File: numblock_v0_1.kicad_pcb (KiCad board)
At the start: 2 copper layers, 100 x 100 mm, 66 parts, among them J1 Conn_01x14_Female, J2 Conn_01x14_Female, J3 Conn_01x05_Female, J4 Conn_02x03_Odd_Even, J5 Conn_01x03_Female, SW1 SW_PUSH-MX_W_LED, SW10 SW_PUSH-MX_W_LED, SW11 SW_PUSH-MX_W_LED, SW12 SW_PUSH-MX_W_LED, SW13 SW_PUSH-MX_W_LED, SW14 SW_PUSH-MX_W_LED, SW15 SW_PUSH-MX_W_LED, SW16 SW_PUSH-MX_W_LED, SW17 SW_PUSH-MX_W_LED, SW18 SW_PUSH-MX_W_LED, SW19 SW_PUSH-MX_W_LED, SW2 SW_PUSH-MX_W_LED, SW20 SW_PUSH-MX_W_LED, SW21 Rotary_Encoder_Switch, SW3 SW_PUSH-MX_W_LED, SW4 SW_PUSH-MX_W_LED, SW5 SW_PUSH-MX_W_LED, SW6 SW_PUSH-MX_W_LED, SW7 SW_PUSH-MX_W_LED, SW8 SW_PUSH-MX_W_LED, SW9 SW_PUSH-MX_W_LED

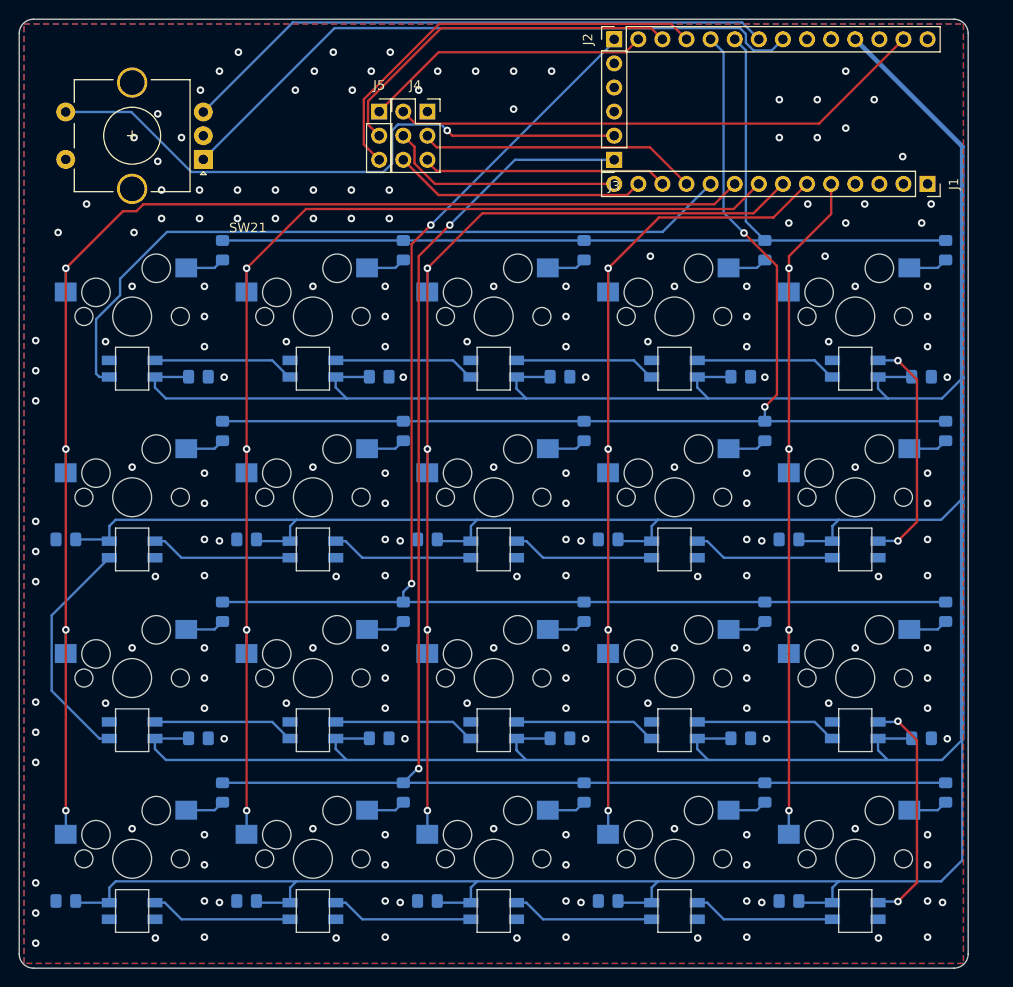
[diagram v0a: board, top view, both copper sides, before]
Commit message: Fixed missing gnd connections
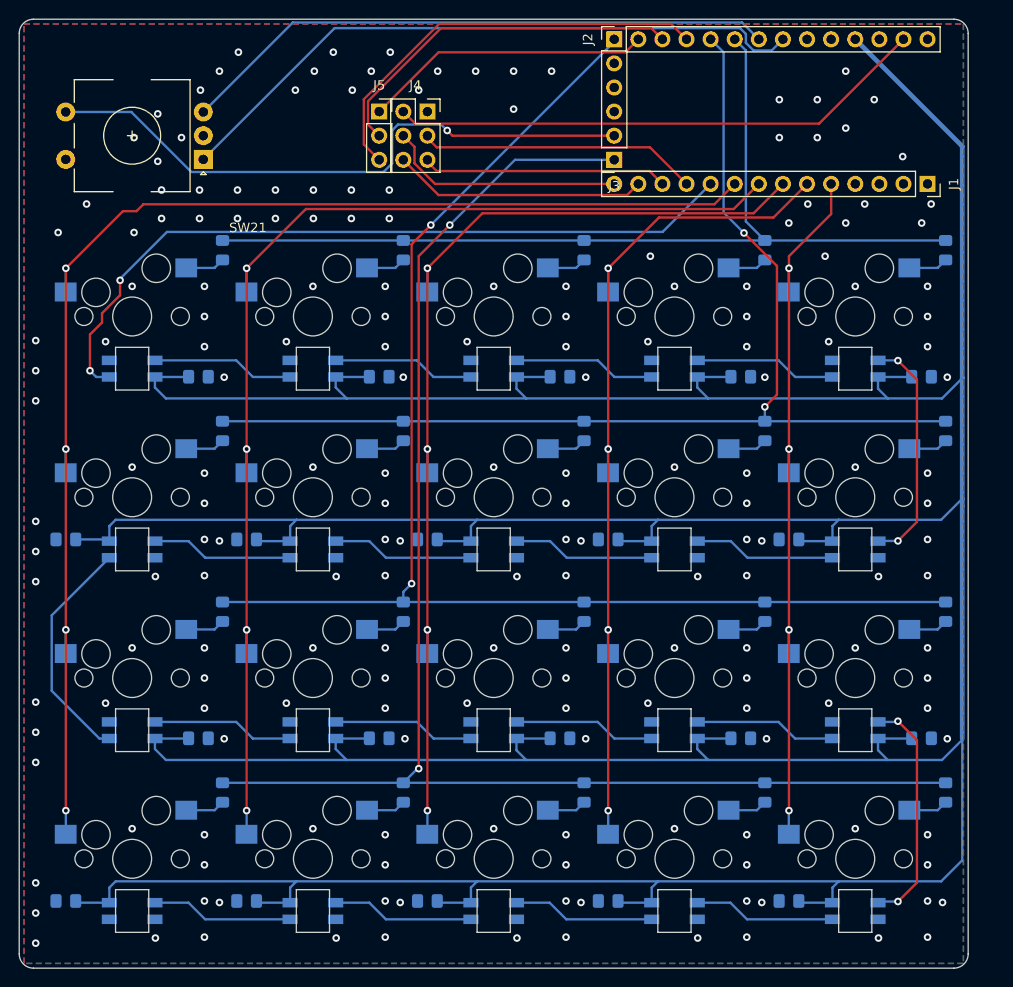
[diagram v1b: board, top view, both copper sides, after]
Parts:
- SW21: footprint Rotary_Encoder:RotaryEncoder_Alps_EC11E-Switch_Vertical_H20mm_CircularMountingHoles -> sofle RGB:RotaryEncoder_Alps_EC11E-Switch_Vertical_H20mm_NoMountingHoles
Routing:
- net /LED: track 79.0 -> 79.5 mm, vias 0 -> 2
- net GND: vias 162 -> 163
- net /R2: vias 3 -> 2

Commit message: kinda done, about to add jumpers for rot. enc.
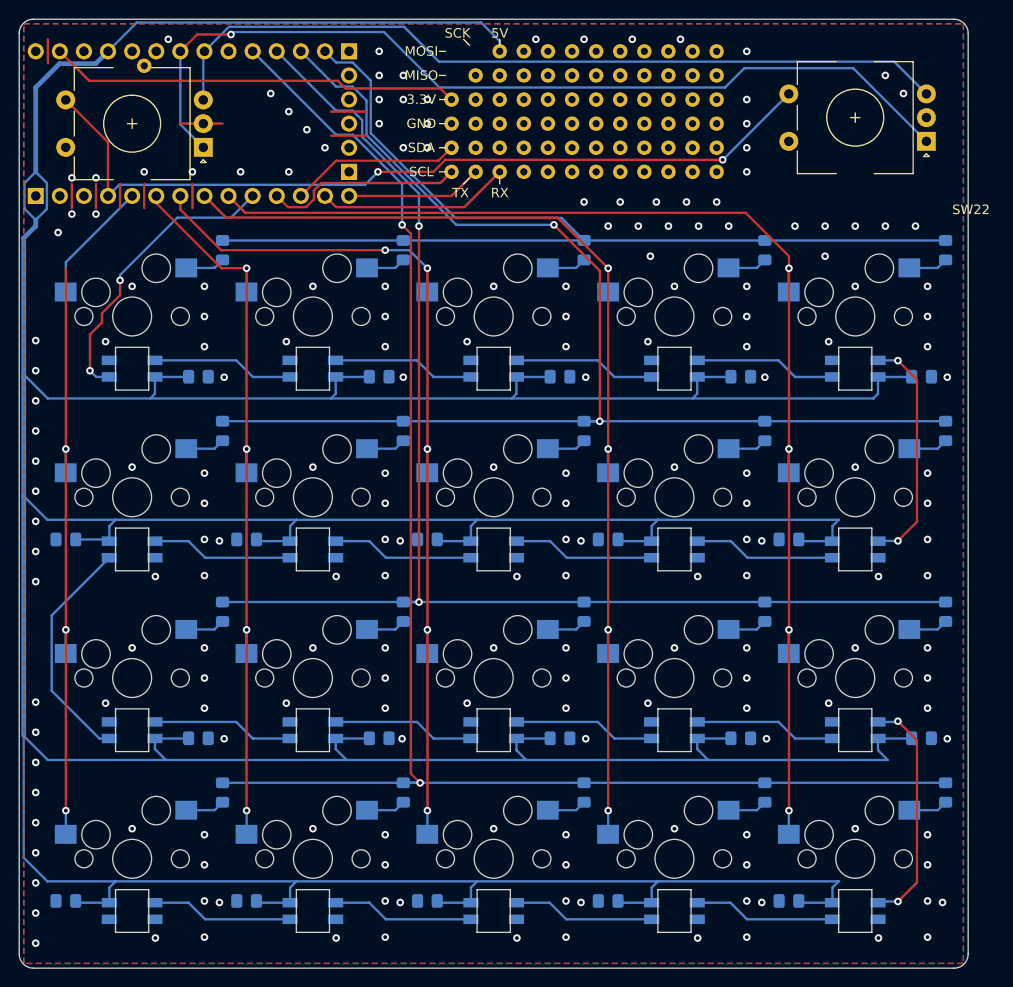
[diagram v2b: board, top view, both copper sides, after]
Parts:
- removed the C1 at (31.1, 118.7)
- removed the C10 at (121.3, 101.6)
- removed the C2 at (50.2, 118.7)
- removed the C3 at (69.2, 118.7)
- removed the C4 at (88.3, 118.7)
- removed the C5 at (107.3, 118.7)
- removed the C6 at (45.1, 101.6)
- removed the C7 at (64.1, 101.6)
- removed the C8 at (83.2, 101.6)
- removed the C9 at (102.2, 101.6)
- removed J4: Conn_02x03_Odd_Even, Connector_PinSocket_2.54mm:PinSocket_2x03_P2.54mm_Vertical
- removed J5: Conn_01x03_Female, Connector_PinSocket_2.54mm:PinSocket_1x03_P2.54mm_Vertical
- added C11: C, Capacitor_SMD:C_0805_2012Metric_Pad1.18x1.45mm_HandSolder, B.Cu at (45.1, 101.6)
- added C12: C, Capacitor_SMD:C_0805_2012Metric_Pad1.18x1.45mm_HandSolder, B.Cu at (64.1, 101.6)
- added C13: C, Capacitor_SMD:C_0805_2012Metric_Pad1.18x1.45mm_HandSolder, B.Cu at (102.2, 101.6)
- added C14: C, Capacitor_SMD:C_0805_2012Metric_Pad1.18x1.45mm_HandSolder, B.Cu at (83.2, 101.6)
- added C15: C, Capacitor_SMD:C_0805_2012Metric_Pad1.18x1.45mm_HandSolder, B.Cu at (121.3, 101.6)
- added C16: C, Capacitor_SMD:C_0805_2012Metric_Pad1.18x1.45mm_HandSolder, B.Cu at (31.1, 118.7)
- added C17: C, Capacitor_SMD:C_0805_2012Metric_Pad1.18x1.45mm_HandSolder, B.Cu at (50.2, 118.7)
- added C18: C, Capacitor_SMD:C_0805_2012Metric_Pad1.18x1.45mm_HandSolder, B.Cu at (69.2, 118.7)
- added C19: C, Capacitor_SMD:C_0805_2012Metric_Pad1.18x1.45mm_HandSolder, B.Cu at (88.3, 118.7)
- added C20: C, Capacitor_SMD:C_0805_2012Metric_Pad1.18x1.45mm_HandSolder, B.Cu at (107.3, 118.7)
- added H1: MountingHole_Pad, sofle RGB:hole_30mil, F.Cu at (71.8, 36.8)
- added H2: MountingHole_Pad, sofle RGB:hole_30mil, F.Cu at (71.8, 34.3)
- added H3: MountingHole_Pad, sofle RGB:hole_30mil, F.Cu at (71.8, 39.4)
- added H4: MountingHole_Pad, sofle RGB:hole_30mil, F.Cu at (71.8, 41.9)
- added H5: MountingHole_Pad, sofle RGB:hole_30mil, F.Cu at (74.3, 41.9)
- added H6: MountingHole_Pad, sofle RGB:hole_30mil, F.Cu at (76.8, 41.9)
- added REF**: hole_30mil, sofle RGB:hole_30mil, F.Cu at (39.4, 30.7)
- added REF**: hole_30mil, sofle RGB:hole_30mil, F.Cu at (87.0, 41.9)
- added REF**: hole_30mil, sofle RGB:hole_30mil, F.Cu at (84.5, 41.9)
- added REF**: hole_30mil, sofle RGB:hole_30mil, F.Cu at (81.9, 41.9)
- added REF**: hole_30mil, sofle RGB:hole_30mil, F.Cu at (79.4, 41.9)
- added REF**: hole_30mil, sofle RGB:hole_30mil, F.Cu at (74.3, 39.4)
- added REF**: hole_30mil, sofle RGB:hole_30mil, F.Cu at (99.7, 39.4)
- added REF**: hole_30mil, sofle RGB:hole_30mil, F.Cu at (97.2, 39.4)
- added REF**: hole_30mil, sofle RGB:hole_30mil, F.Cu at (94.6, 39.4)
- added REF**: hole_30mil, sofle RGB:hole_30mil, F.Cu at (92.1, 39.4)
- added REF**: hole_30mil, sofle RGB:hole_30mil, F.Cu at (89.5, 39.4)
- added REF**: hole_30mil, sofle RGB:hole_30mil, F.Cu at (74.3, 34.3)
- added REF**: hole_30mil, sofle RGB:hole_30mil, F.Cu at (87.0, 39.4)
- added REF**: hole_30mil, sofle RGB:hole_30mil, F.Cu at (84.5, 39.4)
- added REF**: hole_30mil, sofle RGB:hole_30mil, F.Cu at (81.9, 39.4)
- added REF**: hole_30mil, sofle RGB:hole_30mil, F.Cu at (79.4, 39.4)
- added REF**: hole_30mil, sofle RGB:hole_30mil, F.Cu at (76.8, 39.4)
- added REF**: hole_30mil, sofle RGB:hole_30mil, F.Cu at (99.7, 36.8)
- added REF**: hole_30mil, sofle RGB:hole_30mil, F.Cu at (97.2, 36.8)
- added REF**: hole_30mil, sofle RGB:hole_30mil, F.Cu at (94.6, 36.8)
- added REF**: hole_30mil, sofle RGB:hole_30mil, F.Cu at (92.1, 36.8)
- added REF**: hole_30mil, sofle RGB:hole_30mil, F.Cu at (89.5, 36.8)
- added REF**: hole_30mil, sofle RGB:hole_30mil, F.Cu at (74.3, 36.8)
- added REF**: hole_30mil, sofle RGB:hole_30mil, F.Cu at (87.0, 36.8)
- added REF**: hole_30mil, sofle RGB:hole_30mil, F.Cu at (84.5, 36.8)
- added REF**: hole_30mil, sofle RGB:hole_30mil, F.Cu at (81.9, 36.8)
- added REF**: hole_30mil, sofle RGB:hole_30mil, F.Cu at (79.4, 36.8)
- added REF**: hole_30mil, sofle RGB:hole_30mil, F.Cu at (76.8, 36.8)
- added REF**: hole_30mil, sofle RGB:hole_30mil, F.Cu at (99.7, 34.3)
- added REF**: hole_30mil, sofle RGB:hole_30mil, F.Cu at (97.2, 34.3)
- added REF**: hole_30mil, sofle RGB:hole_30mil, F.Cu at (94.6, 34.3)
- added REF**: hole_30mil, sofle RGB:hole_30mil, F.Cu at (92.1, 34.3)
- added REF**: hole_30mil, sofle RGB:hole_30mil, F.Cu at (89.5, 34.3)
- added REF**: hole_30mil, sofle RGB:hole_30mil, F.Cu at (74.3, 31.8)
- added REF**: hole_30mil, sofle RGB:hole_30mil, F.Cu at (87.0, 34.3)
- added REF**: hole_30mil, sofle RGB:hole_30mil, F.Cu at (84.5, 34.3)
- added REF**: hole_30mil, sofle RGB:hole_30mil, F.Cu at (81.9, 34.3)
- added REF**: hole_30mil, sofle RGB:hole_30mil, F.Cu at (79.4, 34.3)
- added REF**: hole_30mil, sofle RGB:hole_30mil, F.Cu at (76.8, 34.3)
- added REF**: hole_30mil, sofle RGB:hole_30mil, F.Cu at (99.7, 31.8)
- added REF**: hole_30mil, sofle RGB:hole_30mil, F.Cu at (97.2, 31.8)
- added REF**: hole_30mil, sofle RGB:hole_30mil, F.Cu at (94.6, 31.8)
- added REF**: hole_30mil, sofle RGB:hole_30mil, F.Cu at (92.1, 31.8)
- added REF**: hole_30mil, sofle RGB:hole_30mil, F.Cu at (89.5, 31.8)
- added REF**: hole_30mil, sofle RGB:hole_30mil, F.Cu at (99.7, 41.9)
- added REF**: hole_30mil, sofle RGB:hole_30mil, F.Cu at (87.0, 31.8)
- added REF**: hole_30mil, sofle RGB:hole_30mil, F.Cu at (84.5, 31.8)
- added REF**: hole_30mil, sofle RGB:hole_30mil, F.Cu at (81.9, 31.8)
- added REF**: hole_30mil, sofle RGB:hole_30mil, F.Cu at (79.4, 31.8)
- added REF**: hole_30mil, sofle RGB:hole_30mil, F.Cu at (76.8, 31.8)
- added REF**: hole_30mil, sofle RGB:hole_30mil, F.Cu at (99.7, 29.2)
- added REF**: hole_30mil, sofle RGB:hole_30mil, F.Cu at (97.2, 29.2)
- added REF**: hole_30mil, sofle RGB:hole_30mil, F.Cu at (94.6, 29.2)
- added REF**: hole_30mil, sofle RGB:hole_30mil, F.Cu at (92.1, 29.2)
- added REF**: hole_30mil, sofle RGB:hole_30mil, F.Cu at (89.5, 29.2)
- added REF**: hole_30mil, sofle RGB:hole_30mil, F.Cu at (97.2, 41.9)
- added REF**: hole_30mil, sofle RGB:hole_30mil, F.Cu at (87.0, 29.2)
- added REF**: hole_30mil, sofle RGB:hole_30mil, F.Cu at (84.5, 29.2)
- added REF**: hole_30mil, sofle RGB:hole_30mil, F.Cu at (81.9, 29.2)
- added REF**: hole_30mil, sofle RGB:hole_30mil, F.Cu at (79.4, 29.2)
- added REF**: hole_30mil, sofle RGB:hole_30mil, F.Cu at (76.8, 29.2)
- added REF**: hole_30mil, sofle RGB:hole_30mil, F.Cu at (94.6, 41.9)
- added REF**: hole_30mil, sofle RGB:hole_30mil, F.Cu at (92.1, 41.9)
- added REF**: hole_30mil, sofle RGB:hole_30mil, F.Cu at (89.5, 41.9)
- added SW22: Rotary_Encoder_Switch, sofle RGB:RotaryEncoder_Alps_EC11E-Switch_Vertical_H20mm_NoMountingHoles, F.Cu at (114.3, 36.2)
- J1, J2, J3: moved to B.Cu
- moved J1 94.0 mm to (27.9, 44.5)
- moved J2 28.0 mm to (61.0, 29.2)
- moved J3 28.0 mm to (61.0, 41.9), turned to 0 degrees
- moved C2 22.1 mm to (64.1, 63.5), turned to 0 degrees
- moved C7 22.1 mm to (50.2, 80.6), turned to 180 degrees
- moved C1 22.1 mm to (45.1, 63.5), turned to 0 degrees
- moved C10 22.1 mm to (107.3, 80.6), turned to 180 degrees
- moved C3 22.1 mm to (83.2, 63.5), turned to 0 degrees
- moved C4 22.1 mm to (102.2, 63.5), turned to 0 degrees
- moved C5 22.1 mm to (121.3, 63.5), turned to 0 degrees
- moved C6 22.1 mm to (31.1, 80.6), turned to 180 degrees
- moved C8 22.1 mm to (69.2, 80.6), turned to 180 degrees
- moved C9 22.1 mm to (88.3, 80.6), turned to 180 degrees
- moved SW21 1.27 mm to (38.1, 36.8)
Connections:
- J1 pad 4: Net-(J1-Pad4) -> /SW
- J1 pad 5: /C5 -> /C1
- J1 pad 6: /C4 -> /C2
- J1 pad 8: /C2 -> /C4
- J1 pad 9: /C1 -> /C5
- J2 pad 1: /R3 -> Net-(J2-Pad1)
- J2 pad 2: /MISO -> /R1
- J2 pad 3: /MOSI -> /R2
- J2 pad 4: /SCK -> /R3
- J2 pad 5: /R2 -> /R4
- J2 pad 6: /R1 -> Net-(J2-Pad6)
- J3 pad 1: /R4 -> Net-(J3-Pad1)
- J3 pad 2: /SW -> Net-(J3-Pad2)
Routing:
- net /C1: track 141.3 -> 77.7 mm, vias 4 -> 3
- net +5V: track 565.3 -> 621.8 mm
- net /C5: track 77.9 -> 130.1 mm
- net /LED: track 79.5 -> 31.1 mm
- net /SCK: track 45.0 -> 0.00 mm
- net /C2: track 124.8 -> 80.3 mm
- net /MOSI: track 38.8 -> 0.00 mm
- net /MISO: track 30.5 -> 0.00 mm
- net /Rot1: track 68.9 -> 97.0 mm, vias 0 -> 1
- net GND: track 0.00 -> 27.3 mm, vias 163 -> 199
- net /SW: track 65.0 -> 88.2 mm, vias 1 -> 2
- net /Rot2: track 63.2 -> 85.2 mm
- net /C4: track 91.8 -> 112.9 mm
- net /R2: track 119.9 -> 136.9 mm
- net /R1: track 98.7 -> 115.0 mm
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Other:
- board text added: "3.3V"
- board text added: "5V"
- board text added: "GND"
- board text added: "MISO"
- board text added: "MOSI"
- board text added: "RX"
- board text added: "SCK"
- board text added: "SCL"
- board text added: "SDA"
- board text added: "TX"

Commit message: done for tonight
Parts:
- removed the REF** at (39.4, 30.7)
- removed the REF** at (81.9, 41.9)
- removed the REF** at (79.4, 41.9)
- removed the REF** at (97.2, 31.8)
- removed the REF** at (84.5, 29.2)
- removed the REF** at (81.9, 29.2)
- removed the REF** at (79.4, 29.2)
- added H10: MountingHole_Pad, sofle RGB:hole_30mil, F.Cu at (81.9, 29.2)
- added H11: MountingHole_Pad, sofle RGB:hole_30mil, F.Cu at (81.9, 41.9)
- added H12: MountingHole_Pad, sofle RGB:hole_30mil, F.Cu at (79.4, 41.9)
- added H13: MountingHole_Pad, sofle RGB:hole_30mil, F.Cu at (79.4, 29.2)
- added H14: MountingHole_Pad, sofle RGB:hole_30mil, F.Cu at (87.0, 29.2)
- added H15: MountingHole_Pad, sofle RGB:hole_30mil, F.Cu at (76.8, 29.2)
- added H7: MountingHole_Pad, sofle RGB:hole_30mil, F.Cu at (71.8, 31.8)
- added H8: MountingHole_Pad, sofle RGB:hole_30mil, F.Cu at (74.3, 29.2)
- added H9: MountingHole_Pad, sofle RGB:hole_30mil, F.Cu at (84.5, 29.2)
- SW22: footprint sofle RGB:RotaryEncoder_Alps_EC11E-Switch_Vertical_H20mm_NoMountingHoles -> Rotary_Encoder:RotaryEncoder_Alps_EC11E-Switch_Vertical_H20mm_CircularMountingHoles
- moved REF** 10.5 mm to (97.2, 31.8)
- moved REF** 5.08 mm to (71.8, 29.2)
- moved SW22 0.63 mm to (114.3, 36.8)
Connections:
- J2 pad 10: Net-(J2-Pad10) -> /A0
- J2 pad 6: Net-(J2-Pad6) -> /Rot2
- J2 pad 7: /Rot2 -> /Rot1
- J2 pad 8: /Rot1 -> /A2
- J2 pad 9: Net-(J2-Pad9) -> /A1
- SW22 pad A: /Rot1 -> Net-(H10-Pad1)
- SW22 pad B: /Rot2 -> Net-(H14-Pad1)
- SW22 pad S1: /SW -> GND
- SW22 pad S2: GND -> Net-(H11-Pad1)
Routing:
- net GND: track 27.3 -> 239.7 mm, vias 199 -> 207
- net Net-(H10-Pad1): track 0.00 -> 45.0 mm
- net /Rot2: track 85.2 -> 40.5 mm
- net /Rot1: track 97.0 -> 57.7 mm
- net Net-(H14-Pad1): track 0.00 -> 38.0 mm
- net /A1: track 0.00 -> 36.3 mm
- net /A2: track 0.00 -> 35.8 mm
- net /A0: track 0.00 -> 35.1 mm
- net /SW: track 88.2 -> 57.9 mm
- net Net-(H11-Pad1): track 0.00 -> 26.5 mm
- net +5V: track 621.8 -> 616.1 mm
- net /C1: track 77.7 -> 77.1 mm, vias 3 -> 4
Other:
- board text added: "A0"
- board text added: "A1"
- board text added: "A2"
- board text added: "A3"
- board text added: "A4"
- board text added: "D13"
- board text added: "VHI!"
- board text removed: "5V"
- board text removed: "MISO"
- board text removed: "MOSI"
- board text removed: "SCK"

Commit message: about to add underglow
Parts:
- D1, D10, D11, D12, D13, D14, D15, D16, D17, D18, D19, D2, D20, D3, D4, D5, D6, D7, D8, D9: footprint Diode_SMD:D_0805_2012Metric_Pad1.15x1.40mm_HandSolder -> Diode_SMD:D_SOD-123
- moved D11 2.01 mm to (49.5, 87.6), turned to 0 degrees
- moved D12 2.01 mm to (68.6, 87.6), turned to 0 degrees
- moved D13 2.01 mm to (87.6, 87.6), turned to 0 degrees
- moved D14 2.01 mm to (106.7, 87.6), turned to 0 degrees
- moved D6 2.01 mm to (49.5, 68.6), turned to 0 degrees
- moved D7 2.01 mm to (68.6, 68.6), turned to 0 degrees
- moved D8 2.01 mm to (87.6, 68.6), turned to 0 degrees
- moved D9 2.01 mm to (106.7, 68.6), turned to 0 degrees
- moved D1 2.01 mm to (49.5, 49.5), turned to 0 degrees
- moved D2 2.01 mm to (68.6, 49.5), turned to 0 degrees
- moved D3 2.01 mm to (87.6, 49.5), turned to 0 degrees
- moved D4 2.01 mm to (106.7, 49.5), turned to 0 degrees
- moved D16 2.01 mm to (49.5, 106.7), turned to 0 degrees
- moved D17 2.01 mm to (68.6, 106.7), turned to 0 degrees
- moved D18 2.01 mm to (87.6, 106.7), turned to 0 degrees
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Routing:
- net /R4: track 163.4 -> 159.9 mm
- net /R2: track 136.9 -> 133.7 mm
- net /R3: track 143.1 -> 139.9 mm
- net +5V: track 616.1 -> 614.6 mm
- net /R1: track 115.0 -> 116.3 mm
- net Net-(D12-Pad1): track 4.17 -> 5.12 mm
- net Net-(D13-Pad1): track 4.17 -> 5.12 mm
- net Net-(D11-Pad1): track 4.17 -> 5.12 mm
- net Net-(D7-Pad1): track 4.17 -> 5.12 mm
- net Net-(D2-Pad1): track 4.17 -> 5.12 mm
- net Net-(D17-Pad1): track 4.17 -> 5.12 mm
- net Net-(D8-Pad1): track 4.17 -> 5.12 mm
- net Net-(D3-Pad1): track 4.17 -> 5.12 mm
- net Net-(D18-Pad1): track 4.17 -> 5.12 mm
- net Net-(D14-Pad1): track 4.17 -> 5.12 mm
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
